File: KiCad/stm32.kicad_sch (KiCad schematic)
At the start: 19 parts, among them J15 Conn_02x05_Odd_Even, J17 Conn_01x04, J18 Conn_01x04, U7 STM32F030C8Tx, Y1 25MHz

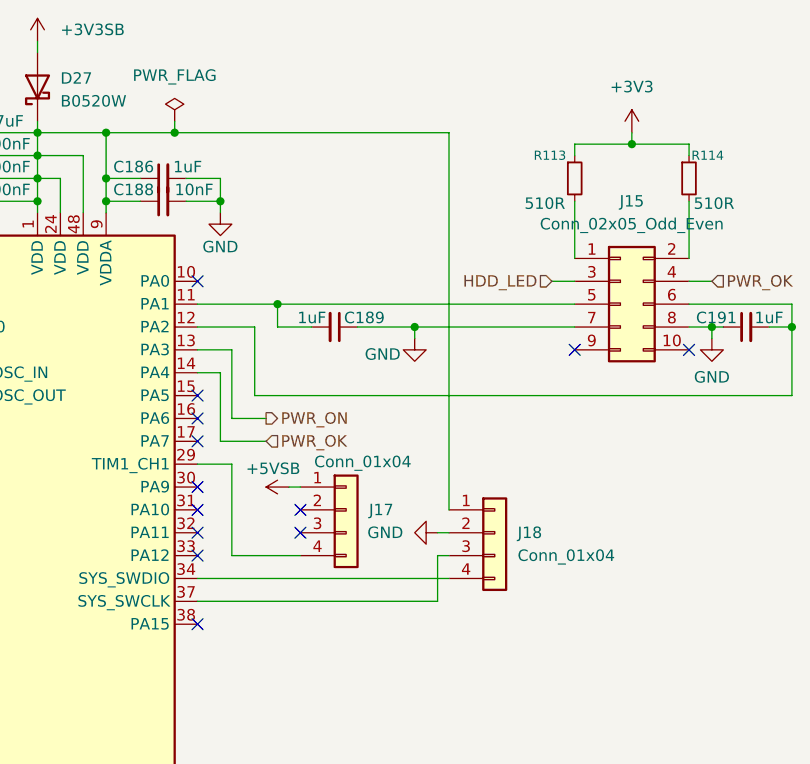
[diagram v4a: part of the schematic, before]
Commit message: Lay out Headers
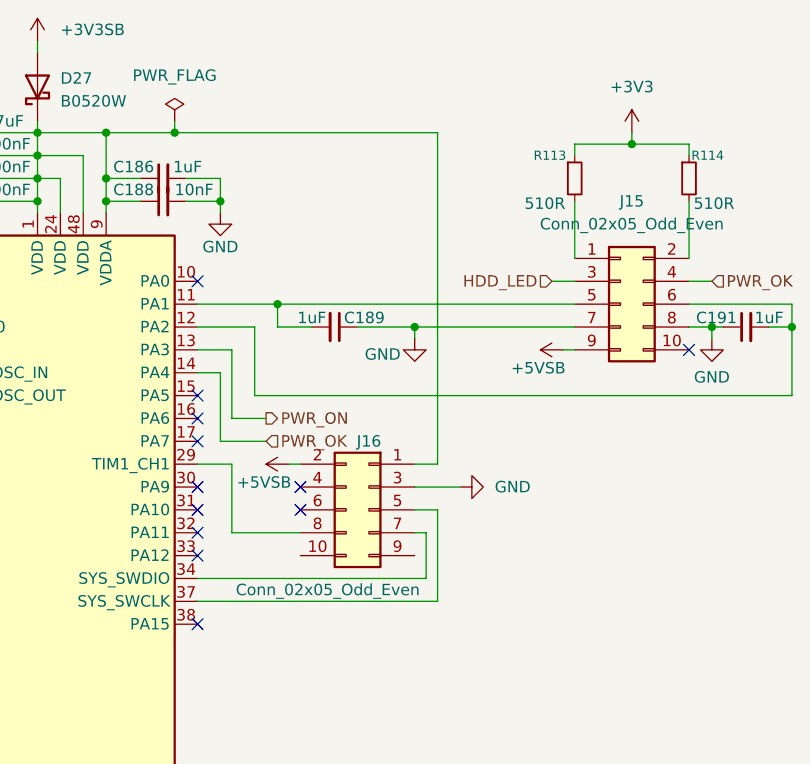
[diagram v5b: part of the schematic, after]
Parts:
- removed J17, J18: Conn_01x04, Connector_PinHeader_2.54mm:PinHeader_1x04_P2.54mm_Vertical, symbol Connector_Generic:Conn_01x04
- added J16: Conn_02x05_Odd_Even, Connector_PinHeader_2.54mm:PinHeader_2x05_P2.54mm_Vertical, symbol Connector_Generic:Conn_02x05_Odd_Even
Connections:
- net +5VSB: now also J15.9 (Pin_9), J16.2 (Pin_2)
- net GND: now also J16.3 (Pin_3)
- net at C183.2, C184.2, C185.2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: now also J16.1 (Pin_1)
- net at U7.37 (PA14): now also J16.5 (Pin_5)
- net at U7.34 (PA13): now also J16.7 (Pin_7)
- net at U7.29 (PA8): now also J16.8 (Pin_8)
- no-connect marks 20 -> 19

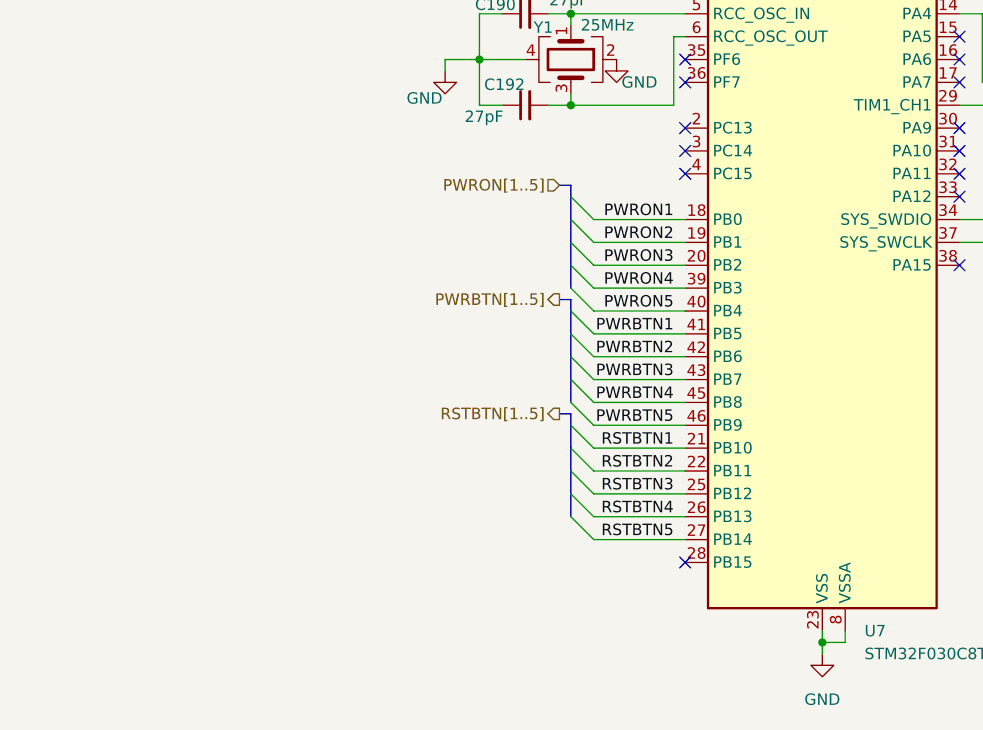
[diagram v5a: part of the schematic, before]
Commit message: Copy modules 2 and 3, remove unnecessary pages
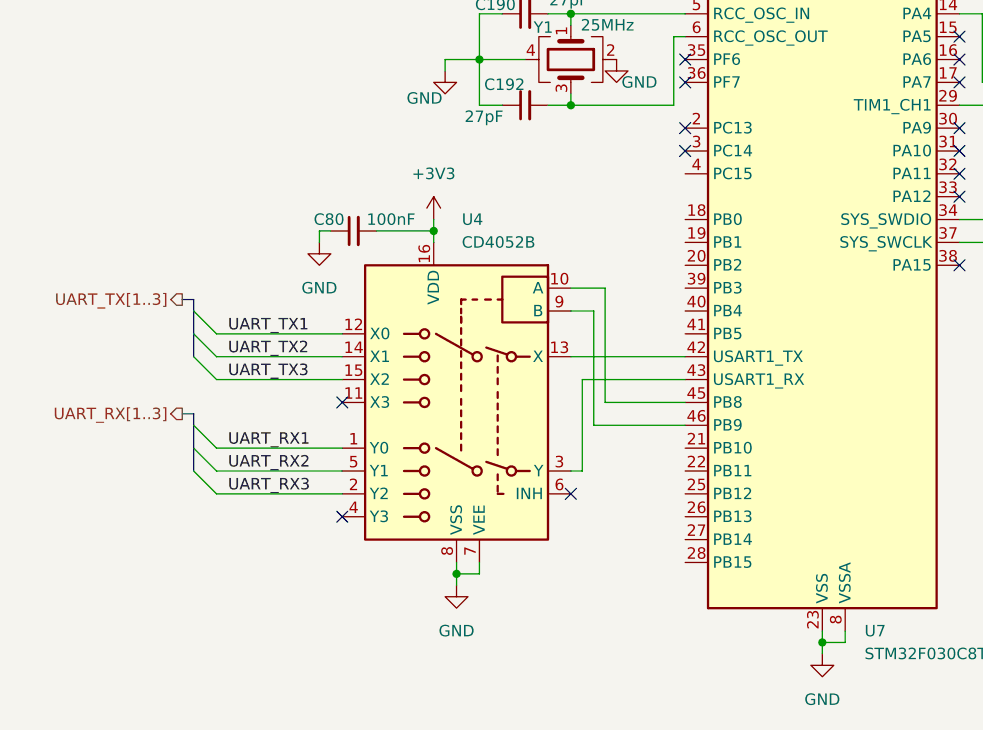
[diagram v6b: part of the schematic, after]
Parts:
- added C80: 100nF, Capacitor_SMD:C_0402_1005Metric, symbol Device:C_Small
- added U4: CD4052B, symbol Analog_Switch:CD4052B
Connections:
- net +3V3: now also C80.2, U4.16 (VDD)
- net GND: now also C80.1, U4.7 (VEE), U4.8 (VSS)
- net PWRBTN1: no longer names the net of U7.41 (PB5)
- net PWRBTN2: no longer names the net of U7.42 (PB6)
- net PWRBTN2: now also U4.13 (X)
- net PWRBTN3: no longer names the net of U7.43 (PB7)
- net PWRBTN3: now also U4.3 (Y)
- net PWRBTN4: no longer names the net of U7.45 (PB8)
- net PWRBTN4: now also U4.10 (A)
- net PWRBTN5: no longer names the net of U7.46 (PB9)
- net PWRBTN5: now also U4.9 (B)
- net PWRON1: no longer names the net of U7.18 (PB0)
- net PWRON2: no longer names the net of U7.19 (PB1)
- net PWRON3: no longer names the net of U7.20 (PB2)
- net PWRON4: no longer names the net of U7.39 (PB3)
- net PWRON5: no longer names the net of U7.40 (PB4)
- net RSTBTN1: no longer names the net of U7.21 (PB10)
- net RSTBTN2: no longer names the net of U7.22 (PB11)
- net RSTBTN3: no longer names the net of U7.25 (PB12)
- net RSTBTN4: no longer names the net of U7.26 (PB13)
- net RSTBTN5: no longer names the net of U7.27 (PB14)
- new net UART_RX1: U4.1 (Y0)
- new net UART_RX2: U4.5 (Y1)
- new net UART_RX3: U4.2 (Y2)
- new net UART_TX1: U4.12 (X0)
- new net UART_TX2: U4.14 (X1)
- new net UART_TX3: U4.15 (X2)
- no-connect marks 19 -> 20

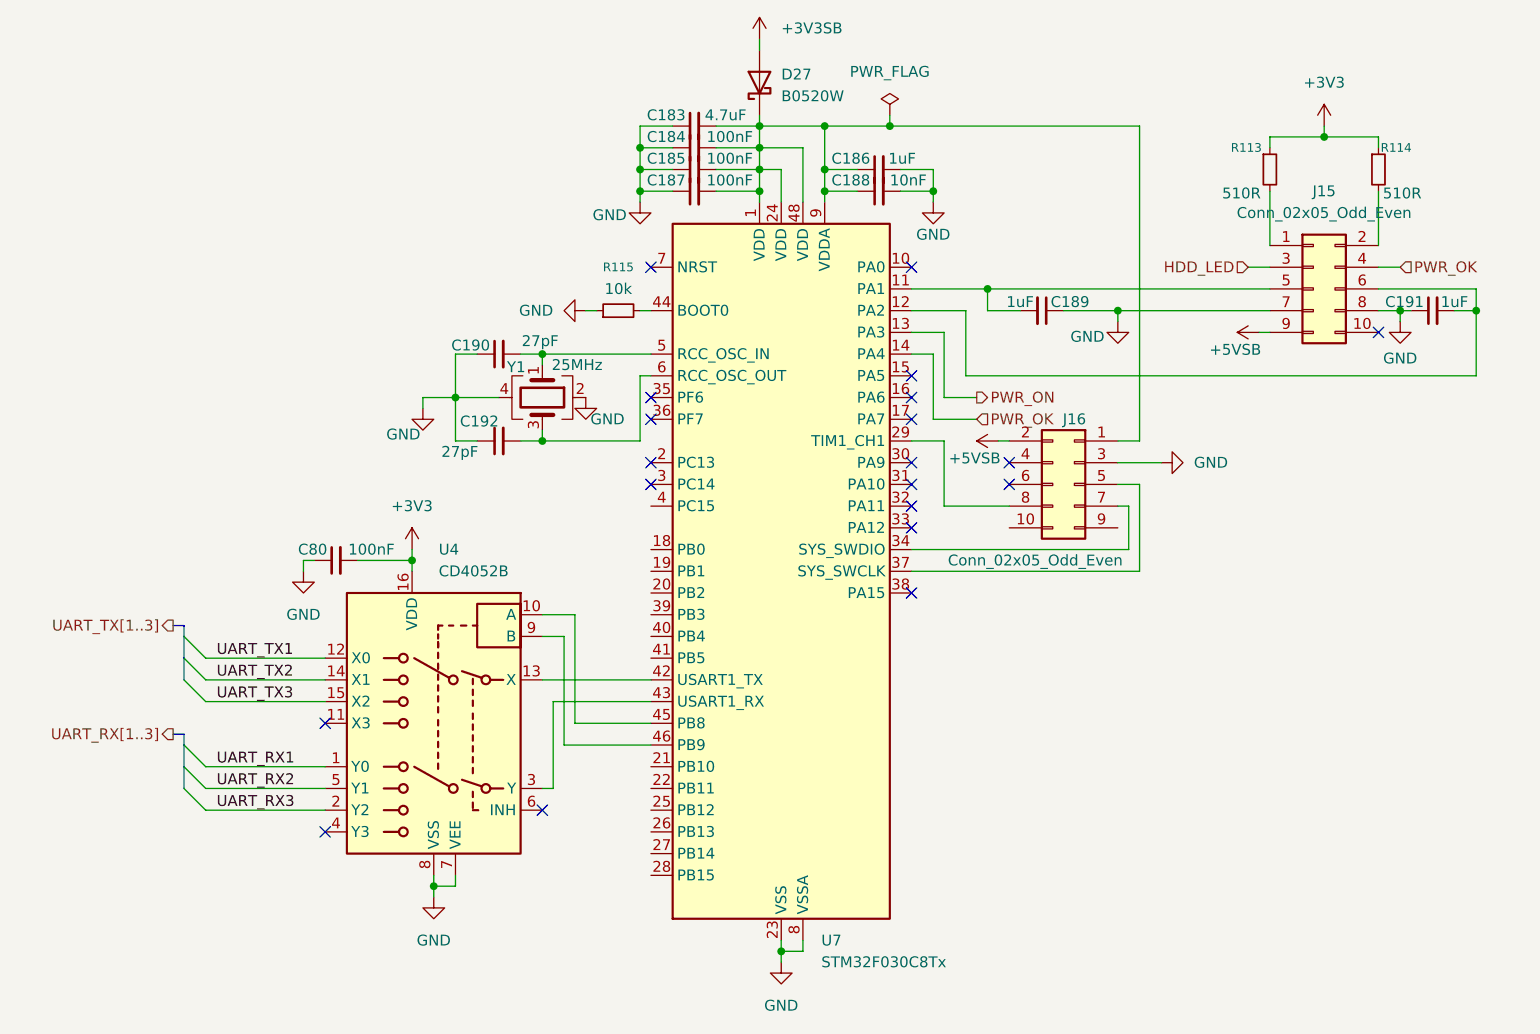
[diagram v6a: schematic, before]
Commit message: Swap stm32 for extra uart port
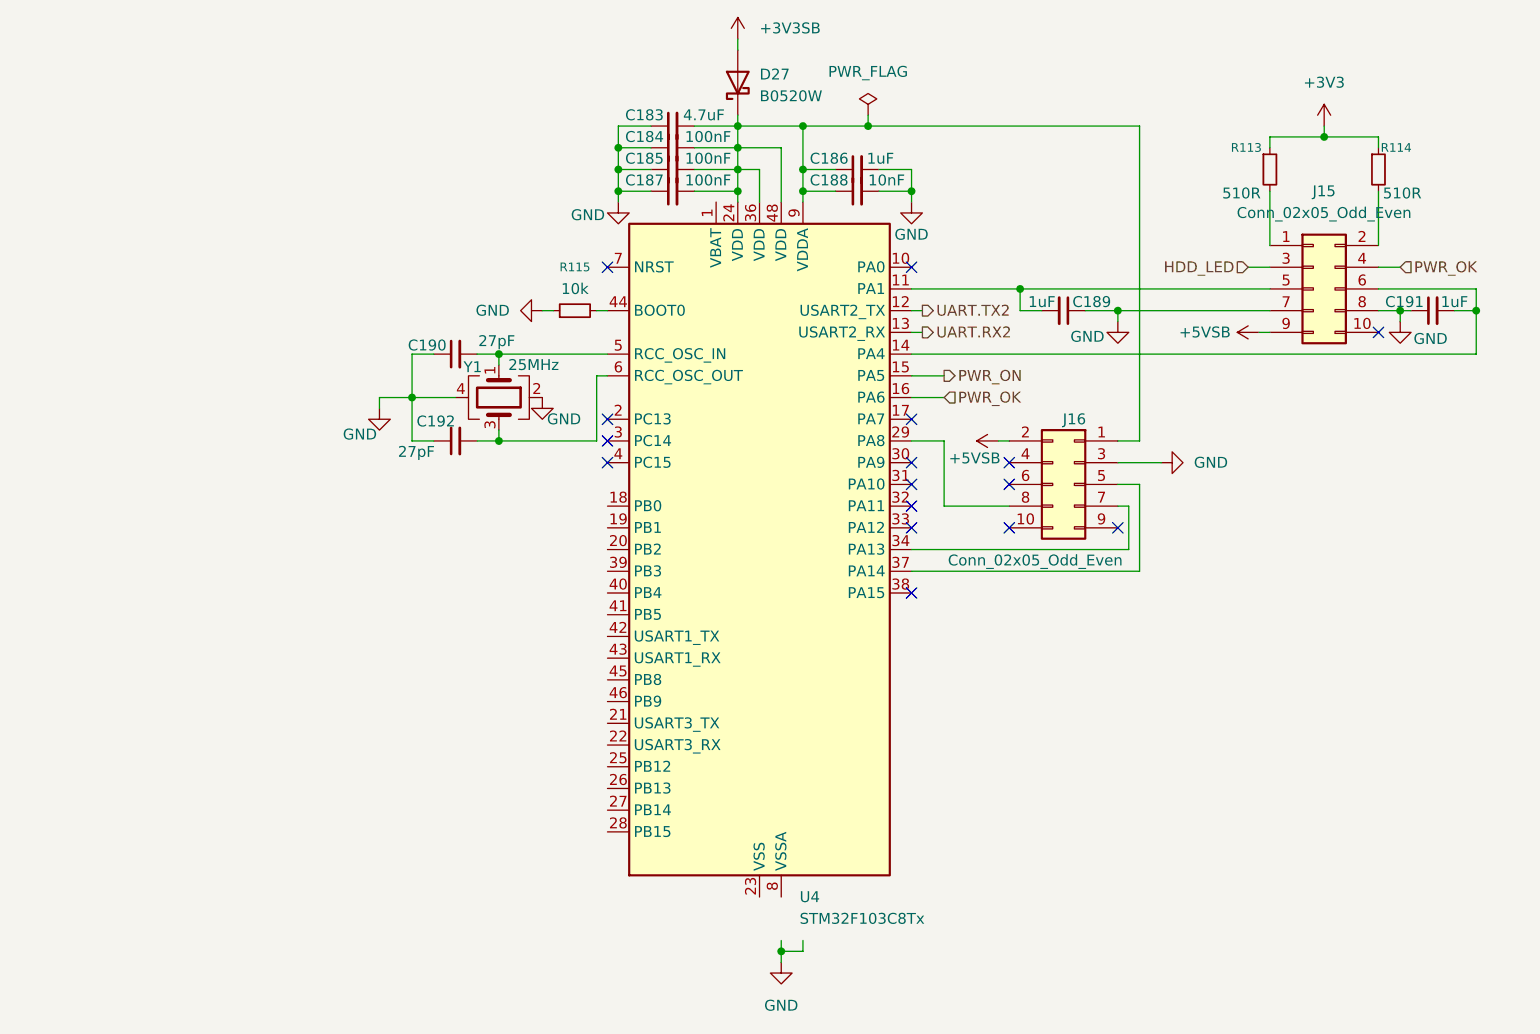
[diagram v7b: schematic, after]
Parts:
- removed C80: 100nF, Capacitor_SMD:C_0402_1005Metric, symbol Device:C_Small
- removed U4: CD4052B, symbol Analog_Switch:CD4052B
- removed U7: STM32F030C8Tx, Package_QFP:LQFP-48_7x7mm_P0.5mm, symbol MCU_ST_STM32F0:STM32F030C8Tx
- added U4: STM32F103C8Tx, Package_QFP:LQFP-48_7x7mm_P0.5mm, symbol MCU_ST_STM32F1:STM32F103C8Tx
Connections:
- net PWR_OK: now also U4.16 (PA6)
- net PWR_ON: now also U4.15 (PA5)
- net at C183.2, C184.2, C185.2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: now also U4.24 (VDD), U4.36 (VDD), U4.48 (VDD), U4.9 (VDDA)
- net at R115.2: now also U4.44 (BOOT0)
- net at C189.2, J15.5 (Pin_5): now also U4.11 (PA1)
- net at C191.2, J15.6 (Pin_6): now also U4.14 (PA4)
- net at C192.2, Y1.3: now also U4.6 (PD1)
- net at J16.8 (Pin_8): now also U4.29 (PA8)
- net at J16.7 (Pin_7): now also U4.34 (PA13)
- net at J16.5 (Pin_5): now also U4.37 (PA14)
- net at C190.2, Y1.1: now also U4.5 (PD0)
- new net: U4.23 (VSS), U4.35 (VSS), U4.47 (VSS)
- new net UART.RX2: U4.13 (PA3)
- new net UART.TX2: U4.12 (PA2)
- no-connect marks 20 -> 16
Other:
- moved on the sheet: C183, C184, C185, C186, C187, C188, C189, C190, C192, D27, R115, Y1
